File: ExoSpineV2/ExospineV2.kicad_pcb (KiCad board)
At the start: 2 copper layers, 79.2 x 74.3 mm, 57 parts, among them J1 GPIO, J11 JST PH 3pin, J12 2.54mm 4pin, J13 JST PH 5pin, J2 Screw Terminal 2pin 5mm, J21 JST PH 2pin, J22 JST PH 2pin, J23 JST PH 2pin, J3 Mounting Hole 2.7mm, J31 JST PH 3pin, J32 JST PH 3pin, J33 JST PH 3pin, J34 JST PH 3pin, J35 JST PH 3pin, J36 JST PH 3pin, J4 Mounting Hole 2.7mm, J5 Mounting Hole 2.7mm, J51 JST PH 2pin, J6 Mounting Hole 2.7mm, J61 JST PH 2pin, J71 JST PH 4pin, J72 JST PH 3pin, J73 JST PH 4pin, J74 JST PH 3pin, J75 JST PH 4pin, J76 JST PH 3pin, J77 JST PH 4pin, J78 JST PH 3pin, J81 JST PH 3pin, J82 JST PH 3pin, U1 MCP3008-I/SL, U2 74HC00D,653, U3 74HC00D,653

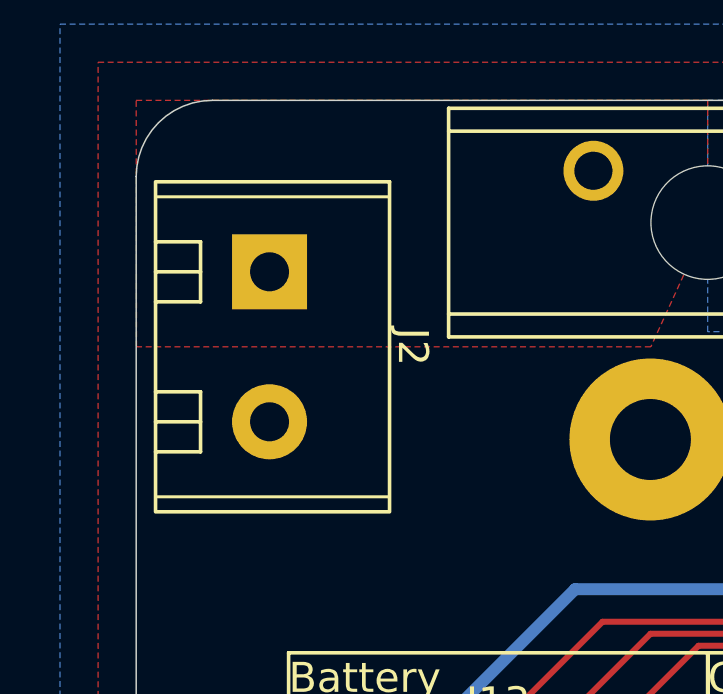
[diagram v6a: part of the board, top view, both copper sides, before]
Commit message: fixed problem with the screw terminal
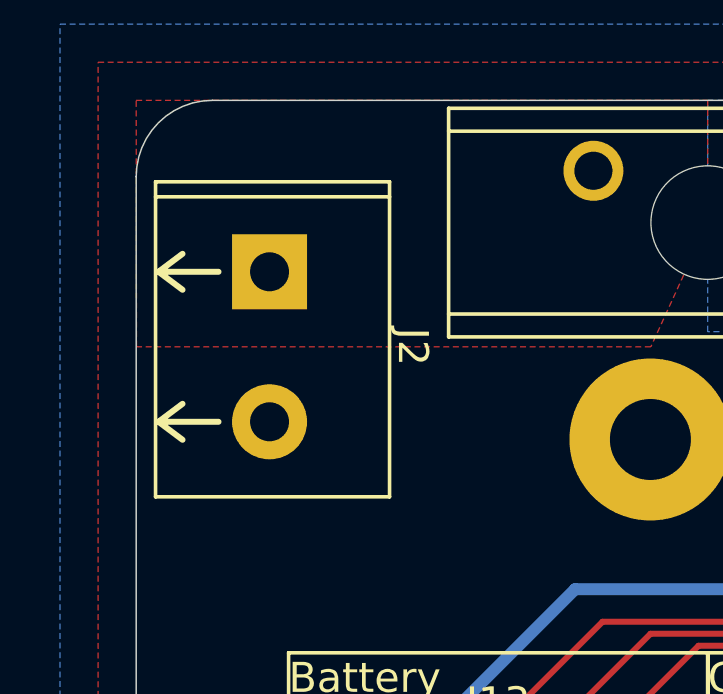
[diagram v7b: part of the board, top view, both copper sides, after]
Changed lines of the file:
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@@
 			(sketchpadsonfab no)
 			(subtractmaskfromsilk no)
-			(outputformat 4)
+			(outputformat 1)
 			(mirror no)
 			(drillshape 0)
@@
 			)
 		)
-		(property "JLCPCB Part Number" "C557646"
+		(property "JLCPCB Part Number" "C5188434"
 			(at 0 0 -90)
 			(unlocked yes)
@@
 		(attr through_hole)
 		(fp_line
-			(start -3.5 3.8)
-			(end -3.5 2.3)
+			(start 5 3.8)
+			(end -5.5 3.8)
 			(stroke
 				(width 0.12)
@@
 		)
 		(fp_line
-			(start -2.5 3.8)
-			(end -2.5 2.3)
-			(stroke
-				(width 0.12)
+			(start -2.5 3.7)
+			(end -1.9 2.9)
+			(stroke
+				(width 0.2)
 				(type default)
 			)
@@
 		)
 		(fp_line
-			(start -1.5 3.8)
-			(end -1.5 2.3)
-			(stroke
-				(width 0.12)
+			(start -2.5 3.7)
+			(end -2.5 1.7)
+			(stroke
+				(width 0.2)
 				(type default)
 			)
@@
 		)
 		(fp_line
-			(start 1.5 3.8)
-			(end 1.5 2.3)
-			(stroke
-				(width 0.12)
+			(start 2.5 3.7)
+			(end 3.1 2.9)
+			(stroke
+				(width 0.2)
 				(type default)
 			)
@@
 		)
 		(fp_line
-			(start 2.5 3.8)
-			(end 2.5 2.3)
-			(stroke
-				(width 0.12)
+			(start 2.5 3.7)
+			(end 2.5 1.7)
+			(stroke
+				(width 0.2)
 				(type default)
 			)
@@
 		)
 		(fp_line
-			(start 3.5 3.8)
-			(end 3.5 2.3)
-			(stroke
-				(width 0.12)
+			(start -3.1 2.9)
+			(end -2.5 3.7)
+			(stroke
+				(width 0.2)
 				(type default)
 			)
@@
 		)
 		(fp_line
-			(start -1.5 2.3)
-			(end -3.5 2.3)
-			(stroke
-				(width 0.12)
+			(start 1.9 2.9)
+			(end 2.5 3.7)
+			(stroke
+				(width 0.2)
 				(type default)
 			)
@@
 		)
 		(fp_line
-			(start 3.5 2.3)
-			(end 1.5 2.3)
+			(start -5.5 -4)
+			(end -5.5 3.8)
 			(stroke
 				(width 0.12)
@@
 			(end -5 3.8)
 			(stroke
-				(width 0.1)
+				(width 0.12)
 				(type default)
 			)
@@
 			(end 5 3.8)
 			(stroke
-				(width 0.1)
+				(width 0.12)
 				(type default)
 			)
 			(layer "F.SilkS")
 		)
-		(fp_rect
-			(start -5.5 -4)
-			(end 5.5 3.8)
+		(fp_line
+			(start 5 -4)
+			(end -5.5 -4)
 			(stroke
 				(width 0.12)
 				(type default)
 			)
-			(fill none)
 			(layer "F.SilkS")
 		)
@@
 			(pintype "passive")
 		)
+		(model "${KIPRJMOD}/ExoSpineV2.pretty/[EasyEDA]MX126-5.0-02P-GN01-Cu-S-A.step"
+			(offset
+				(xyz 0 0 -1.6)
+			)
+			(scale
+				(xyz 1 1 1)
+			)
+			(rotate
+				(xyz 0 0 0)
+			)
+		)
 	)
